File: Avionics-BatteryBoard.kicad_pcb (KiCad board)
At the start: 4 copper layers, 90.2 x 95.9 mm, 133 parts, among them J5 Fuel Gauge Programming Header, J6 205338-0002, J7 205338-0004, J9 522711069, Q1 SIRA99DP-T1-GE3, Q10 SIRA99DP-T1-GE3, Q11 MBT2222ADW1T1, Q12 NX3008NBKS, Q13 MBT2222ADW1T1, Q14 NX3008NBKS, Q2 IRLML2803, Q3 SIRA99DP-T1-GE3, Q4 IRLML2803, Q5 SIRA99DP-T1-GE3, Q6 IRLML2803, Q7 SIRA99DP-T1-GE3, Q8 SIRA99DP-T1-GE3, Q9 SIRA99DP-T1-GE3, U1 S-8209AAA-T8T1U, U10 TLX9000, U2 S-8209AAA-T8T1U, U3 LTC4412xS6, U4 LTC4412xS6, U5 MAX17205, U6 D5V0P4UR6SO, U7 D5V0P4UR6SO, U8 TLX9000, U9 TLX9000

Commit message: placing components
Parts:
- removed the R64 at (123.9, 102.2)
- removed the R65 at (128.7, 102.2)
- added R64: 0R, Resistor_SMD:R_0603_1608Metric, B.Cu at (324.0, 74.2)
- added R64: 0R, Resistor_SMD:R_0603_1608Metric, B.Cu at (124.8, 103.9)
- added R65: 0R, Resistor_SMD:R_0603_1608Metric, B.Cu at (324.0, 76.7)
- added R65: 0R, Resistor_SMD:R_0603_1608Metric, B.Cu at (124.8, 108.7)
- moved TP1 202.1 mm to (306.0, 86.0), turned to 180 degrees
- moved C14 201.8 mm to (304.3, 45.7), turned to 180 degrees
- moved TP2 201.4 mm to (306.0, 89.5), turned to 180 degrees
- moved U6 195.8 mm to (300.0, 52.3), turned to 180 degrees
- moved U7 193.9 mm to (300.0, 57.0), turned to 180 degrees
- moved Q5 171.4 mm to (290.9, 42.9), turned to 180 degrees
- moved R26 167.1 mm to (293.4, 52.5)
- moved R24 166.7 mm to (293.4, 47.4), turned to 180 degrees
- moved R27 164.8 mm to (293.4, 55.0), turned to 180 degrees
- moved F10 164.7 mm to (284.1, 41.3), turned to 180 degrees
- moved D5 164.4 mm to (284.8, 44.2)
- moved R25 164.4 mm to (293.4, 49.9), turned to 180 degrees
- moved Q6 163.2 mm to (288.9, 52.6), turned to 180 degrees
- moved U9 160.2 mm to (286.6, 48.3), turned to 180 degrees
- moved Q1 148.9 mm to (291.4, 65.5), turned to 180 degrees
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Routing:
- net /Battery Bus Protection/DISCHARGE_ACTIVE: track 119.5 -> 0.00 mm, vias 2 -> 0
- net /Battery Bus Protection/CHARGE_ACTIVE: track 103.2 -> 0.00 mm, vias 2 -> 0
- net Net-(U5-AIN1): track 91.0 -> 0.00 mm, vias 2 -> 0
- net /Interfaces/HEATER0_ON: track 81.4 -> 0.00 mm, vias 2 -> 0
- net +3V3: track 78.9 -> 0.00 mm, vias 9 -> 1
- net /Interfaces/HEATER1_ON: track 64.4 -> 0.00 mm, vias 2 -> 0
- net /Interfaces/ALERT: track 59.1 -> 0.00 mm, vias 2 -> 0
- net /Interfaces/HEATER_ENABLE: track 56.7 -> 0.00 mm, vias 2 -> 0
- net /Battery Bus Detection/CHARGE_EN: track 53.3 -> 0.00 mm, vias 2 -> 0
- net Net-(U5-AIN2): track 34.7 -> 0.00 mm, vias 2 -> 0
- net SYSTEM_VDD: track 32.6 -> 0.00 mm, vias 2 -> 0
- net /Battery Bus Detection/DISCHARGE_EN: track 31.1 -> 0.00 mm, vias 3 -> 0
- net /Interfaces/SDA_BUS: track 35.8 -> 8.71 mm, vias 0 -> 1
- net /Battery Monitor/SDA: track 23.8 -> 0.00 mm, vias 2 -> 0
- net /Battery Monitor/SCL: track 21.5 -> 0.00 mm
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- removed copper zone on B.Cu, net +3V3
- removed copper zone on B.Cu, net /Battery Bus Detection/BATT_N
- removed copper zone on In1.Cu, net /Battery Bus Detection/BATT_N
- removed copper zone on B.Cu, net /Battery Bus Detection/BATT_P
- removed copper zone on In2.Cu, net /Battery Bus Detection/BATT_P
- removed copper zone on B.Cu, net /Battery Temperature Protection/BatteryHeater/V_HEATER
- removed copper zone on B.Cu, net /Battery Temperature Protection/BatteryHeater1/V_HEATER
- removed copper zone on B.Cu, net GND
- removed copper zone on B.Cu, net Net-(F10-Pad2)
- removed copper zone on B.Cu, net Net-(F11-Pad2)
- removed copper zone on B.Cu, net Net-(F8-Pad1)
- removed copper zone on B.Cu, net Net-(F9-Pad1)
- removed copper zone on B.Cu, net Net-(J11-neg3)
- removed copper zone on B.Cu, net Net-(J11-neg4)
- removed copper zone on B.Cu, net Net-(J11-pos1)
- removed copper zone on B.Cu, net Net-(J11-pos2)
- removed copper zone on B.Cu, net Net-(Q10-D)
- removed copper zone on B.Cu, net Net-(Q7-D)
- removed copper zone on B.Cu, net Net-(U3-SENSE)
- removed copper zone on B.Cu, net SYSTEM_VDD
- removed copper zone on B.Cu, net SYSTEM_VSS
- removed copper zone on B.Cu, net VBUS

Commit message: uhh idk
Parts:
- moved R24 181.5 mm to (125.7, 117.0)
- moved R25 179.8 mm to (129.0, 123.0)
- moved Q6 176.7 mm to (125.7, 120.2), turned to -90 degrees
- moved Q5 175.0 mm to (133.8, 119.9), turned to -90 degrees
- moved U9 172.1 mm to (129.2, 117.9), turned to 90 degrees
- moved R26 170.6 mm to (134.9, 115.6)
- moved R27 168.7 mm to (138.3, 121.2), turned to 0 degrees
- moved D5 166.3 mm to (138.3, 122.7)
- moved R7 162.6 mm to (134.3, 101.3)
- moved R8 160.3 mm to (137.4, 107.5)
- moved F10 158.9 mm to (141.5, 111.4), turned to -90 degrees
- moved Q2 157.8 mm to (134.3, 104.4), turned to -90 degrees
- moved Q1 154.3 mm to (142.1, 104.5), turned to -90 degrees
- moved R9 152.7 mm to (143.2, 100.2)
- moved U8 152.6 mm to (137.6, 102.1), turned to 90 degrees
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
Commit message: started routing
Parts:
- removed C12, C13: 10n, Capacitor_SMD:C_0603_1608Metric
- removed Q11, Q13: MBT2222ADW1T1, Package_TO_SOT_SMD:SOT-363_SC-70-6
- removed Q12, Q14: NX3008NBKS, Package_TO_SOT_SMD:SOT-363_SC-70-6
- removed R54, R55, R59, R60: 10k, Resistor_SMD:R_0603_1608Metric
- removed R56, R61: 680R, Resistor_SMD:R_0603_1608Metric
- removed R57, R62: 100k, Resistor_SMD:R_0603_1608Metric
- removed R58, R63: 200k, Resistor_SMD:R_0603_1608Metric
- removed R64 (x2), R65 (x2): 0R, Resistor_SMD:R_0603_1608Metric
- moved TP1 204.3 mm to (103.1, 110.5)
- moved TP2 204.3 mm to (103.1, 113.8)
- moved C14 201.5 mm to (108.5, 93.3), turned to -90 degrees
- moved U6 196.2 mm to (109.7, 100.3), turned to 0 degrees
- moved U7 194.4 mm to (109.7, 96.9), turned to 0 degrees
- moved D6 144.6 mm to (168.8, 96.8), turned to 90 degrees
- moved F9 26.9 mm to (139.7, 97.5), turned to 90 degrees
- moved F8 21.8 mm to (154.5, 82.8), turned to 90 degrees
- moved R67 20.1 mm to (150.9, 84.1), turned to 0 degrees
- moved F10 18.6 mm to (123.0, 113.9)
- moved R14 17.9 mm to (142.4, 125.7), turned to 180 degrees
- moved Q9 17.8 mm to (152.2, 88.1), turned to 180 degrees
- moved D4 17.5 mm to (142.4, 124.2), turned to 0 degrees
- moved Q10 16.3 mm to (152.1, 96.1), turned to 180 degrees
- moved F7 15.9 mm to (159.8, 82.8)
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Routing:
- net /Battery Monitor/I2C Protection/SDA_DEVICE: track 12.3 -> 0.00 mm, vias 1 -> 0
- net /Battery Monitor/I2C Protection/SCL_DEVICE: track 12.2 -> 0.00 mm, vias 1 -> 0
- net Net-(Q13B-B2): track 9.81 -> 0.00 mm
- net Net-(Q11B-B2): track 9.72 -> 0.00 mm
- net Net-(U5-CELL1): track 0.00 -> 9.19 mm, vias 0 -> 2
- net /Interfaces/SDA_BUS: track 8.71 -> 0.00 mm, vias 1 -> 0
- net GND: track 8.59 -> 0.00 mm, vias 4 -> 0
- net Net-(U5-VBATT): track 0.00 -> 7.90 mm
- net /Battery Bus Detection/BATT_N: track 0.00 -> 6.08 mm
- net SYSTEM_VSS: track 0.00 -> 6.03 mm
- net Net-(Q12B-G): track 4.76 -> 0.00 mm
- net Net-(Q14B-G): track 4.67 -> 0.00 mm
- net /Interfaces/SCL_BUS: track 3.84 -> 0.00 mm, vias 1 -> 0
- net Net-(Q13A-B1): track 2.93 -> 0.00 mm
- net Net-(Q11A-B1): track 2.74 -> 0.00 mm
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- added copper zone on B.Cu, net /Battery Bus Detection/BATT_N
- added copper zone on B.Cu, net /Battery Bus Detection/BATT_P
- added copper zone on B.Cu, net Net-(J11-neg3)
- added copper zone on B.Cu, net Net-(J11-neg4)
- added copper zone on B.Cu, net Net-(J11-pos1)
- added copper zone on B.Cu, net Net-(J11-pos2)

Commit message: still routing
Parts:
- added C12: 10n, Capacitor_SMD:C_0603_1608Metric, B.Cu at (116.6, 101.6)
- added C13: 10n, Capacitor_SMD:C_0603_1608Metric, B.Cu at (126.7, 108.2)
- added Q11: MBT2222ADW1T1, Package_TO_SOT_SMD:SOT-363_SC-70-6, B.Cu at (123.7, 102.5)
- added Q12: NX3008NBKS, Package_TO_SOT_SMD:SOT-363_SC-70-6, B.Cu at (119.5, 102.5)
- added Q13: MBT2222ADW1T1, Package_TO_SOT_SMD:SOT-363_SC-70-6, B.Cu at (119.5, 107.3)
- added Q14: NX3008NBKS, Package_TO_SOT_SMD:SOT-363_SC-70-6, B.Cu at (123.7, 107.3)
- added R54: 10k, Resistor_SMD:R_0603_1608Metric, B.Cu at (127.4, 102.5)
- added R55: 10k, Resistor_SMD:R_0603_1608Metric, B.Cu at (119.6, 104.9)
- added R56: 680R, Resistor_SMD:R_0603_1608Metric, B.Cu at (125.9, 102.5)
- added R57: 100k, Resistor_SMD:R_0603_1608Metric, B.Cu at (116.6, 104.9)
- added R58: 200k, Resistor_SMD:R_0603_1608Metric, B.Cu at (116.6, 103.4)
- added R59: 10k, Resistor_SMD:R_0603_1608Metric, B.Cu at (115.8, 107.3)
- added R60: 10k, Resistor_SMD:R_0603_1608Metric, B.Cu at (123.6, 104.9)
- added R61: 680R, Resistor_SMD:R_0603_1608Metric, B.Cu at (117.3, 107.3)
- added R62: 100k, Resistor_SMD:R_0603_1608Metric, B.Cu at (126.7, 104.9)
- added R63: 200k, Resistor_SMD:R_0603_1608Metric, B.Cu at (126.7, 106.4)
- added R64: 0R, Resistor_SMD:R_0603_1608Metric, B.Cu at (121.6, 102.5)
- added R65: 0R, Resistor_SMD:R_0603_1608Metric, B.Cu at (121.6, 107.3)
- moved C5 4.78 mm to (163.8, 102.7), turned to 180 degrees
- moved R10 3.14 mm to (143.0, 112.4), turned to 0 degrees
- moved Q2 3.10 mm to (133.7, 106.4)
- moved R9 3.10 mm to (142.8, 102.2)
- moved F9 3.10 mm to (140.1, 100.5)
- moved Q1 3.10 mm to (141.6, 106.5)
- moved R8 3.10 mm to (136.8, 109.4)
- moved U8 3.10 mm to (137.1, 104.1)
- moved R7 3.10 mm to (133.8, 103.3)
- moved D3 3.04 mm to (143.0, 110.8), turned to 180 degrees
- moved U3 2.90 mm to (163.6, 99.9), turned to 90 degrees
- moved C6 2.55 mm to (150.4, 99.9), turned to -90 degrees
- moved U4 2.31 mm to (152.8, 100.0), turned to -90 degrees
- moved R46 2.11 mm to (123.3, 81.5)
- moved Q8 1.82 mm to (160.4, 95.0)
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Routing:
- net Net-(U5-AIN1): track 0.00 -> 72.4 mm, vias 0 -> 2
- net /Interfaces/ALERT: track 0.00 -> 36.2 mm, vias 0 -> 2
- net /Battery Monitor/I2C Protection/SDA_DEVICE: track 0.00 -> 24.3 mm, vias 0 -> 3
- net /Battery Bus Detection/CHARGE_EN: track 0.00 -> 23.5 mm, vias 0 -> 2
- net Net-(U5-AIN2): track 0.00 -> 22.8 mm, vias 0 -> 2
- net Net-(U1-DO): track 0.00 -> 21.6 mm, vias 0 -> 2
- net Net-(U1-CO): track 0.00 -> 20.9 mm, vias 0 -> 2
- net /Battery Monitor/I2C Protection/SCL_DEVICE: track 0.00 -> 19.6 mm, vias 0 -> 3
- net /Battery Bus Detection/DISCHARGE_EN: track 0.00 -> 16.8 mm, vias 0 -> 2
- net /Battery Monitor/SDA: track 0.00 -> 13.3 mm
- net /Interfaces/SDA_BUS: track 0.00 -> 12.1 mm, vias 0 -> 1
- net /Battery Monitor/SCL: track 0.00 -> 10.5 mm, vias 0 -> 2
- net Net-(Q13B-B2): track 0.00 -> 9.81 mm
- net Net-(Q11B-B2): track 0.00 -> 9.72 mm
- net GND: track 0.00 -> 8.59 mm, vias 0 -> 5
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- added copper zone on B.Cu, net Net-(F8-Pad1)
- added copper zone on B.Cu, net Net-(Q10-D)
- added copper zone on B.Cu, net Net-(Q7-D)
- added copper zone on B.Cu, net Net-(U3-SENSE)
- added copper zone on B.Cu, net SYSTEM_VSS

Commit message: finished routing
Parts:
- moved C5 5.50 mm to (159.1, 99.8), turned to 90 degrees
- moved TP2 4.99 mm to (106.6, 110.3)
- moved TP1 4.50 mm to (106.6, 113.3)
- moved R40 3.91 mm to (110.0, 110.9)
- moved F9 3.61 mm to (143.7, 100.3), turned to 0 degrees
- moved R37 3.60 mm to (110.0, 112.8)
- moved kibuzzard-6A6B646A 3.59 mm to (98.7, 110.3)
- moved kibuzzard-6786F69C 2.80 mm to (98.7, 113.3)
- moved U3 1.69 mm to (162.0, 99.7), turned to 0 degrees
- moved C6 1.01 mm to (149.4, 99.8), turned to 90 degrees
- moved U4 0.72 mm to (152.2, 99.6), turned to 0 degrees
- moved R11 0.71 mm to (133.6, 118.6)
- moved Q4 0.67 mm to (133.6, 121.8)
- moved C12 0.53 mm to (116.0, 101.6)
- moved C13 0.53 mm to (126.1, 108.2)
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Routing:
- net +3V3: track 0.00 -> 63.9 mm, vias 1 -> 4
- net /Battery Bus Protection/CHARGE_ACTIVE: track 0.00 -> 62.8 mm, vias 0 -> 2
- net /Interfaces/HEATER0_ON: track 3.27 -> 57.0 mm, vias 0 -> 2
- net /Battery Bus Protection/DISCHARGE_ACTIVE: track 0.00 -> 52.0 mm, vias 0 -> 2
- net /Interfaces/HEATER1_ON: track 3.65 -> 34.2 mm, vias 0 -> 2
- net /Interfaces/HEATER_ENABLE: track 5.99 -> 32.1 mm, vias 0 -> 2
- net /Interfaces/SCL_BUS: track 7.25 -> 21.9 mm, vias 1 -> 2
- net /Battery Monitor/SCL: track 10.5 -> 22.6 mm
- net Net-(Q1-G): track 0.00 -> 12.0 mm
- net /Battery Monitor/SDA: track 13.3 -> 25.1 mm
- net /Interfaces/SDA_BUS: track 12.1 -> 23.1 mm, vias 1 -> 2
- net Net-(Q3-G): track 0.00 -> 8.78 mm
- net Net-(Q5-G): track 0.00 -> 8.65 mm
- net /Interfaces/ALERT: track 36.2 -> 42.2 mm
- net Net-(Q8-G): track 0.00 -> 3.67 mm
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- added copper zone on B.Cu, net +3V3
- added copper zone on B.Cu, net /Battery Temperature Protection/BatteryHeater/V_HEATER
- added copper zone on B.Cu, net /Battery Temperature Protection/BatteryHeater1/V_HEATER
- added copper zone on B.Cu, net GND
- added copper zone on B.Cu, net Net-(F10-Pad2)
- added copper zone on B.Cu, net Net-(F11-Pad2)
- added copper zone on B.Cu, net Net-(F9-Pad1)
- added copper zone on B.Cu, net SYSTEM_VDD
- added copper zone on B.Cu, net VBUS

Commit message: made silkscreen better
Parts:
- moved U6 0.61 mm to (110.8, 100.3)
- moved U7 0.61 mm to (110.7, 96.9)
- moved D6 0.33 mm to (168.4, 96.9)
- moved D8 0.13 mm to (166.0, 68.8)
- moved C14 0.07 mm to (109.0, 93.4)
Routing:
- net /Interfaces/HEATER1_ON: track 34.2 -> 35.9 mm
- net /Interfaces/HEATER0_ON: track 57.0 -> 58.6 mm
- net /Interfaces/SDA_BUS: track 23.1 -> 23.6 mm
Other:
- board text added: "ARGUS CubeSat Carnegie Mellon University BatteryBoard v4.0"
- board text added: "batteryboard.v4.1"
- board text removed: "ARGUS CubeSat Carnegie Mellon University BatteryBoard v3.2"

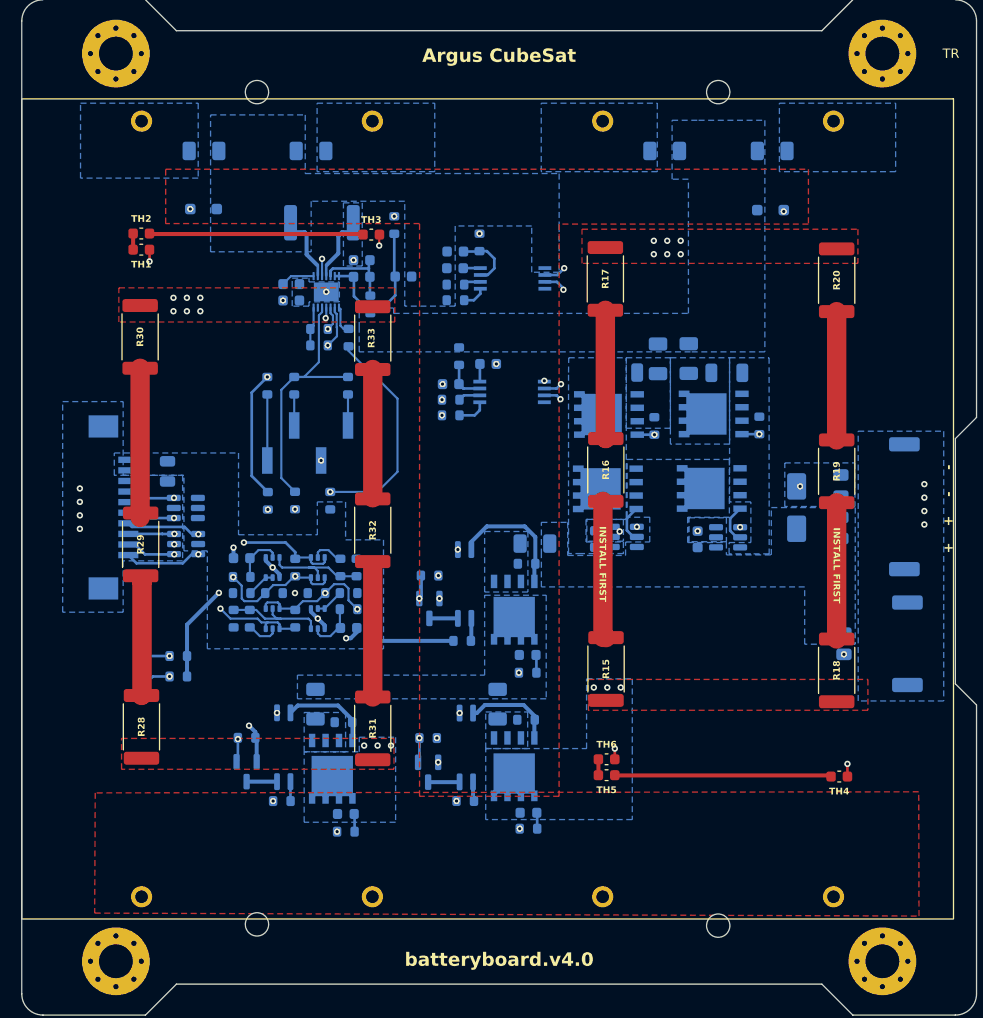
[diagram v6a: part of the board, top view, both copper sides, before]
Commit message: batteryboard v4.0 complete, need to fix footprint courtyard so drc passes but othw should be all good
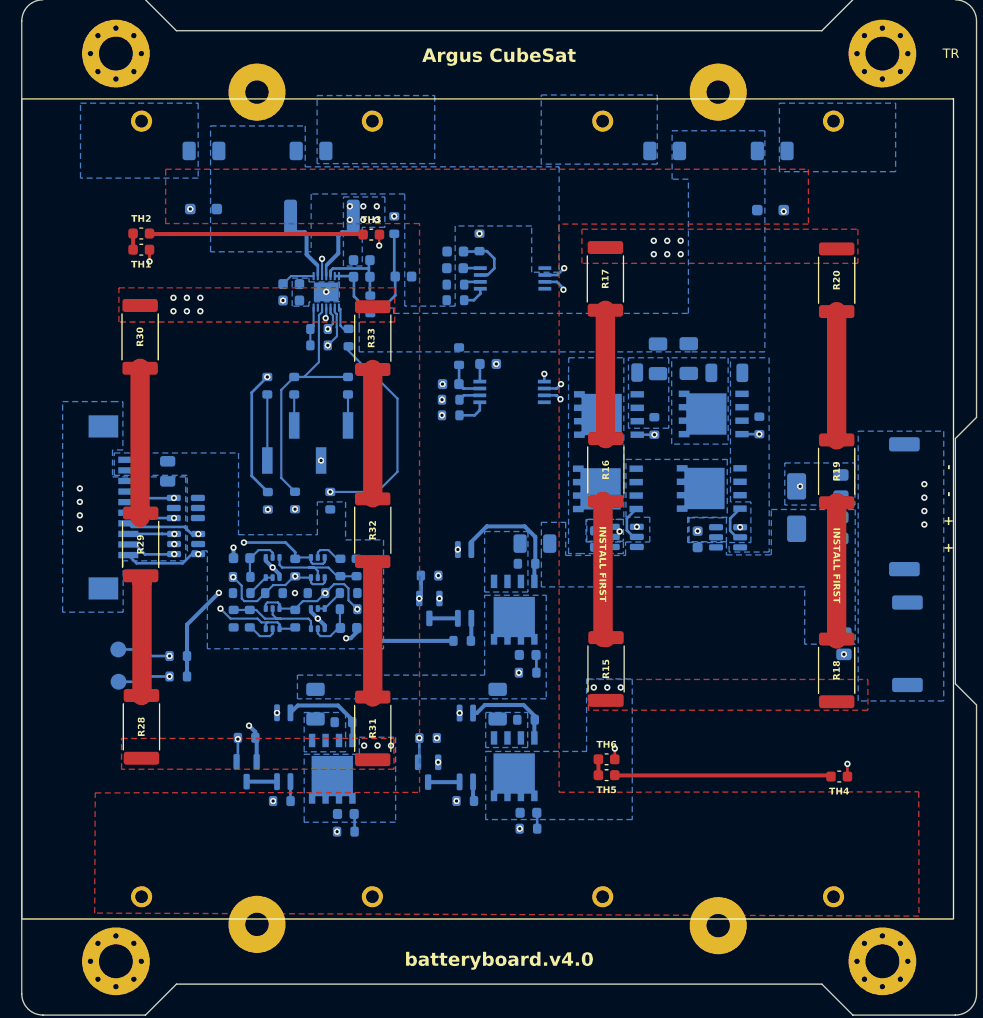
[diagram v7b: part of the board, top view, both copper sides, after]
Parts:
- moved TP1 2.23 mm to (104.4, 113.3)
- moved TP2 2.23 mm to (104.4, 110.3)
- moved kibuzzard-6786F69C 1.07 mm to (99.8, 113.3)
- moved kibuzzard-6A6B646A 1.07 mm to (99.8, 110.2)
- moved R43 0.51 mm to (123.6, 69.4)
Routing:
- net /Battery Bus Protection/DISCHARGE_ACTIVE: track 52.0 -> 54.3 mm
- net /Battery Bus Protection/CHARGE_ACTIVE: track 62.8 -> 65.0 mm
- net /Battery Bus Detection/BATT_M: track 0.00 -> 0.73 mm
- net /Interfaces/ALERT: track 42.2 -> 41.5 mm
- net SYSTEM_VSS: vias 27 -> 32
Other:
- board text removed: "batteryboard.v4.1"

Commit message: fixed up some silkscreen stuff
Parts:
- moved TH1 0.56 mm to (106.6, 73.1)
- moved TH2 0.56 mm to (106.6, 71.5)
- moved TH3 0.56 mm to (128.3, 71.6)
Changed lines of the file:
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@@
 	(footprint "Capacitor_SMD:C_0603_1608Metric"
 		(layer "F.Cu")
-		(at 128.257 71.0706)
+		(at 128.2834 71.6308)
 		(descr "Capacitor SMD 0603 (1608 Metric), square (rectangular) end terminal, IPC-7351 nominal, (Body size source: IPC-SM-782 page 76, https://www.pcb-3d.com/wordpress/wp-content/uploads/ipc-sm-782a_amendment_1_and_2.pdf), generated with kicad-footprint-generator")
 		(tags "capacitor")
@@
 	(footprint "Capacitor_SMD:C_0603_1608Metric"
 		(layer "F.Cu")
-		(at 106.54 72.493 180)
+		(at 106.5664 73.0532 180)
 		(descr "Capacitor SMD 0603 (1608 Metric), square (rectangular) end terminal, IPC-7351 nominal, (Body size source: IPC-SM-782 page 76, https://www.pcb-3d.com/wordpress/wp-content/uploads/ipc-sm-782a_amendment_1_and_2.pdf), generated with kicad-footprint-generator")
 		(tags "capacitor")
@@
 	(footprint "Capacitor_SMD:C_0603_1608Metric"
 		(layer "F.Cu")
-		(at 106.54 70.9676)
+		(at 106.5664 71.5278)
 		(descr "Capacitor SMD 0603 (1608 Metric), square (rectangular) end terminal, IPC-7351 nominal, (Body size source: IPC-SM-782 page 76, https://www.pcb-3d.com/wordpress/wp-content/uploads/ipc-sm-782a_amendment_1_and_2.pdf), generated with kicad-footprint-generator")
 		(tags "capacitor")
@@
 		(layer "Edge.Cuts")
 	)
+	(gr_text "+"
+		(at 240.32 132.01 0)
+		(layer "F.Cu")
+		(effects
+			(font
+				(size 3 3)
+				(thickness 0.3)
+				(bold yes)
+			)
+			(justify left bottom)
+		)
+	)
 	(gr_text "INSTALL FIRST"
-		(at 150.11239 102.18975 270)
+		(at 106.33 90.09 270)
 		(layer "F.SilkS")
 		(effects
@@
 	)
 	(gr_text "INSTALL FIRST"
-		(at 172.21039 102.31675 270)
+		(at 128.428 90.217 270)
 		(layer "F.SilkS")
 		(effects
@@
 	)
 	(gr_text "-"
-		(at 182.753 93.0402 90)
+		(at 106.23983 58.84 0)
 		(layer "F.SilkS")
 		(effects
 			(font
-				(size 0.889 0.889)
-				(thickness 0.1778)
-				(bold yes)
+				(size 5 5)
+				(thickness 0.15)
+			)
+			(justify left bottom)
+		)
+	)
+	(gr_text "+"
+		(at 106.2482 140.6652 0)
+		(layer "F.SilkS")
+		(effects
+			(font
+				(size 5 5)
+				(thickness 0.15)
 			)
+			(justify left bottom)
 		)
 	)
 	(gr_text "-"
-		(at 182.753 95.5802 90)
+		(at 125.109811 58.84 0)
 		(layer "F.SilkS")
 		(effects
 			(font
-				(size 0.889 0.889)
-				(thickness 0.1778)
-				(bold yes)
+				(size 5 5)
+				(thickness 0.15)
 			)
+			(justify left bottom)
 		)
 	)
 	(gr_text "+"
-		(at 182.753 98.1202 90)
+		(at 125.2474 140.6398 0)
 		(layer "F.SilkS")
 		(effects
 			(font
-				(size 0.889 0.889)
-				(thickness 0.1778)
-				(bold yes)
+				(size 5 5)
+				(thickness 0.15)
 			)
+			(justify left bottom)
 		)
 	)
 	(gr_text "+"
-		(at 182.753 100.6602 90)
+		(at 146.9 58.84 0)
 		(layer "F.SilkS")
 		(effects
 			(font
-				(size 0.889 0.889)
-				(thickness 0.1778)
-				(bold yes)
+				(size 5 5)
+				(thickness 0.15)
+			)
+			(justify left bottom)
+		)
+	)
+	(gr_text "-"
+		(at 146.921 140.4 0)
+		(layer "F.SilkS")
+		(effects
+			(font
+				(size 5 5)
+				(thickness 0.15)
+			)
+			(justify left bottom)
+		)
+	)
+	(gr_text "+"
+		(at 168.32 58.84 0)
+		(layer "F.SilkS")
+		(effects
+			(font
+				(size 5 5)
+				(thickness 0.15)
+			)
+			(justify left bottom)
+		)
+	)
+	(gr_text "-"
+		(at 168.32 140.405076 0)
+		(layer "F.SilkS")
+		(effects
+			(font
+				(size 5 5)
+				(thickness 0.15)
 			)
+			(justify left bottom)
 		)
 	)
@@
 	)
 	(segment
-		(start 107.315 71.017)
-		(end 127.379 71.017)
+		(start 107.3414 71.5772)
+		(end 127.4054 71.5772)
 		(width 0.381)
 		(layer "F.Cu")
@@
 	)
 	(segment
-		(start 129.0066 72.1106)
-		(end 129.0066 71.096)
+		(start 129.033 72.6708)
+		(end 129.033 71.6562)
 		(width 0.2032)
 		(layer "F.Cu")
@@
 	)
 	(via
-		(at 129.0066 72.1106)
+		(at 129.033 72.6708)
 		(size 0.6)
 		(drill 0.3)
@@
 	)
 	(segment
-		(start 107.315 72.493)
-		(end 107.315 73.6092)
+		(start 107.3414 73.0532)
+		(end 107.3414 74.1694)
 		(width 0.254)
 		(layer "F.Cu")
@@
 	)
 	(via
-		(at 107.315 73.6092)
+		(at 107.3414 74.1694)
 		(size 0.6)
 		(drill 0.3)
@@
 	)
 	(segment
-		(start 116.8146 79.9846)
-		(end 124.1542 79.9846)
+		(start 112.0902 75.2602)
+		(end 116.8146 79.9846)
 		(width 0.254)
 		(layer "In1.Cu")
@@
 	)
 	(segment
-		(start 112.0902 75.2602)
-		(end 116.8146 79.9846)
+		(start 116.8146 79.9846)
+		(end 124.1542 79.9846)
 		(width 0.254)
 		(layer "In1.Cu")
@@
 	)
 	(segment
-		(start 108.966 75.2602)
-		(end 112.0902 75.2602)
+		(start 107.3414 74.1694)
+		(end 108.4322 75.2602)
 		(width 0.254)
 		(layer "In1.Cu")
@@
 	)
 	(segment
-		(start 107.315 73.6092)
-		(end 108.966 75.2602)
+		(start 108.4322 75.2602)
+		(end 112.0902 75.2602)
 		(width 0.254)
 		(layer "In1.Cu")
@@
 	)
 	(segment
-		(start 105.765 71.017)
-		(end 105.765 72.39)
+		(start 105.7914 71.5772)
+		(end 105.7914 72.9502)
 		(width 0.381)
 		(layer "F.Cu")
@@
 		(hatch edge 0.5)
 		(priority 15)
-		(connect_pads
+		(connect_pads yes
 			(clearance 0.2032)
 		)
@@
 			(thermal_gap 0.5)
 			(thermal_bridge_width 0.5)
+			(smoothing chamfer)
+			(radius 0.254)
 			(island_removal_mode 0)
 		)
